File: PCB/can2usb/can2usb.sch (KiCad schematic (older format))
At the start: 36 parts, among them J1 STLINK, J2 Conn_01x03_Male, P1 USB_C_Plug_USB2.0, SW1 BOOT_SW, U1 STM32F103C6Tx, U2 TLP175A, U3 MCP2561-E-SN, U4 LM1117-3.3, U5 USBLC6-2SC6, Y1 16MHz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

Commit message: Finished brd
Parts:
- removed SW1: BOOT_SW, Button_Switch_SMD:SW_SPDT_PCM12, symbol Switch:SW_SPDT
- added H1, H2, H3: MountingHole, MountingHole:MountingHole_2.2mm_M2, symbol Mechanical:MountingHole
- added JP1: SolderJumper_3_Open, Jumper:SolderJumper-3_P1.3mm_Open_RoundedPad1.0x1.5mm, symbol Jumper:SolderJumper_3_Open
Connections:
- net +3V3: now also JP1.3 (B)
- net GND: now also JP1.1 (A)
- net at R8.2: now also JP1.2 (C)
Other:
- moved on the sheet: R8
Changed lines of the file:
@@
 L power:GND #PWR015
 U 1 1 63317619
-P 1100 6025
-F 0 "#PWR015" H 1100 5775 50  0001 C CNN
-F 1 "GND" V 1105 5897 50  0000 R CNN
-F 2 "" H 1100 6025 50  0001 C CNN
-F 3 "" H 1100 6025 50  0001 C CNN
-	1    1100 6025
+P 1125 6350
+F 0 "#PWR015" H 1125 6100 50  0001 C CNN
+F 1 "GND" V 1130 6222 50  0000 R CNN
+F 2 "" H 1125 6350 50  0001 C CNN
+F 3 "" H 1125 6350 50  0001 C CNN
+	1    1125 6350
 	0    1    1    0
 $EndComp
@@
 L power:+3.3V #PWR014
 U 1 1 63316E56
-P 1100 5825
-F 0 "#PWR014" H 1100 5675 50  0001 C CNN
-F 1 "+3.3V" V 1115 5953 50  0000 L CNN
-F 2 "" H 1100 5825 50  0001 C CNN
-F 3 "" H 1100 5825 50  0001 C CNN
-	1    1100 5825
-	0    -1   -1   0
-$EndComp
-Wire Wire Line
-	1500 5925 1550 5925
+P 1525 6350
+F 0 "#PWR014" H 1525 6200 50  0001 C CNN
+F 1 "+3.3V" V 1540 6478 50  0000 L CNN
+F 2 "" H 1525 6350 50  0001 C CNN
+F 3 "" H 1525 6350 50  0001 C CNN
+	1    1525 6350
+	0    1    1    0
+$EndComp
 $Comp
 L Device:R_Small R8
 U 1 1 6330E866
-P 1650 5925
-F 0 "R8" V 1454 5925 50  0000 C CNN
-F 1 "1k" V 1545 5925 50  0000 C CNN
-F 2 "Resistor_SMD:R_0805_2012Metric" H 1650 5925 50  0001 C CNN
-F 3 "~" H 1650 5925 50  0001 C CNN
-	1    1650 5925
-	0    1    1    0
-$EndComp
-$Comp
-L Switch:SW_SPDT SW1
-U 1 1 6330D3AE
-P 1300 5925
-F 0 "SW1" H 1300 5600 50  0000 C CNN
-F 1 "BOOT_SW" H 1300 5691 50  0000 C CNN
-F 2 "Button_Switch_SMD:SW_SPDT_PCM12" H 1300 5925 50  0001 C CNN
-F 3 "~" H 1300 5925 50  0001 C CNN
-	1    1300 5925
+P 1325 6600
+F 0 "R8" V 1129 6600 50  0000 C CNN
+F 1 "1k" V 1220 6600 50  0000 C CNN
+F 2 "Resistor_SMD:R_0805_2012Metric" H 1325 6600 50  0001 C CNN
+F 3 "~" H 1325 6600 50  0001 C CNN
+	1    1325 6600
 	-1   0    0    1
 $EndComp
@@
 Text GLabel 1475 1875 0    50   Input ~ 0
 BOOT0
-Text GLabel 1750 5925 2    50   Input ~ 0
+Text GLabel 1325 6700 3    50   Input ~ 0
 BOOT0
 Wire Notes Line
@@
 Text Notes 7100 6725 0    50   ~ 0
 USB2CAN - CAN TO UART TRANSLATION
+$Comp
+L Mechanical:MountingHole H1
+U 1 1 6349E742
+P 6625 5875
+F 0 "H1" H 6725 5921 50  0000 L CNN
+F 1 "MountingHole" H 6725 5830 50  0000 L CNN
+F 2 "MountingHole:MountingHole_2.2mm_M2" H 6625 5875 50  0001 C CNN
+F 3 "~" H 6625 5875 50  0001 C CNN
+	1    6625 5875
+	1    0    0    -1
+$EndComp
+$Comp
+L Mechanical:MountingHole H2
+U 1 1 6349F0A8
+P 6625 6225
+F 0 "H2" H 6725 6271 50  0000 L CNN
+F 1 "MountingHole" H 6725 6180 50  0000 L CNN
+F 2 "MountingHole:MountingHole_2.2mm_M2" H 6625 6225 50  0001 C CNN
+F 3 "~" H 6625 6225 50  0001 C CNN
+	1    6625 6225
+	1    0    0    -1
+$EndComp
+$Comp
+L Mechanical:MountingHole H3
+U 1 1 634CAEE0
+P 7650 5850
+F 0 "H3" H 7750 5896 50  0000 L CNN
+F 1 "MountingHole" H 7750 5805 50  0000 L CNN
+F 2 "MountingHole:MountingHole_2.2mm_M2" H 7650 5850 50  0001 C CNN
+F 3 "~" H 7650 5850 50  0001 C CNN
+	1    7650 5850
+	1    0    0    -1
+$EndComp
+$Comp
+L Jumper:SolderJumper_3_Open JP1
+U 1 1 635001D7
+P 1325 6350
+F 0 "JP1" H 1325 6555 50  0000 C CNN
+F 1 "SolderJumper_3_Open" H 1325 6464 50  0000 C CNN
+F 2 "Jumper:SolderJumper-3_P1.3mm_Open_RoundedPad1.0x1.5mm" H 1325 6350 50  0001 C CNN
+F 3 "~" H 1325 6350 50  0001 C CNN
+	1    1325 6350
+	1    0    0    -1
+$EndComp
 $EndSCHEMATC

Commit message: Minor chnages
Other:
- moved on the sheet: H3
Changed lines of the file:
@@
 L Mechanical:MountingHole H3
 U 1 1 634CAEE0
-P 7650 5850
-F 0 "H3" H 7750 5896 50  0000 L CNN
-F 1 "MountingHole" H 7750 5805 50  0000 L CNN
-F 2 "MountingHole:MountingHole_2.2mm_M2" H 7650 5850 50  0001 C CNN
-F 3 "~" H 7650 5850 50  0001 C CNN
-	1    7650 5850
+P 7500 5900
+F 0 "H3" H 7600 5946 50  0000 L CNN
+F 1 "MountingHole" H 7600 5855 50  0000 L CNN
+F 2 "MountingHole:MountingHole_2.2mm_M2" H 7500 5900 50  0001 C CNN
+F 3 "~" H 7500 5900 50  0001 C CNN
+	1    7500 5900
 	1    0    0    -1
 $EndComp

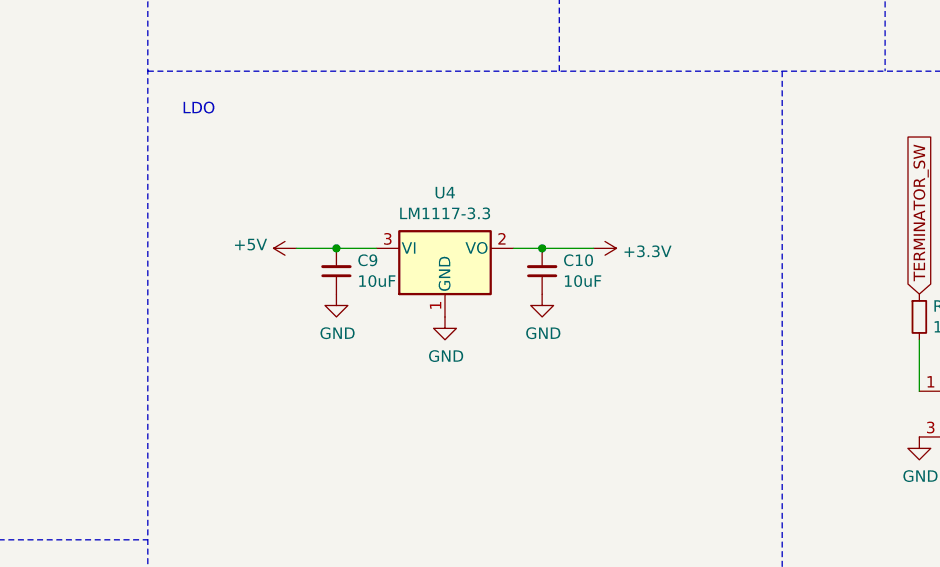
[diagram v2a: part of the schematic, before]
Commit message: New PCB design with 0402 and smaller LDO
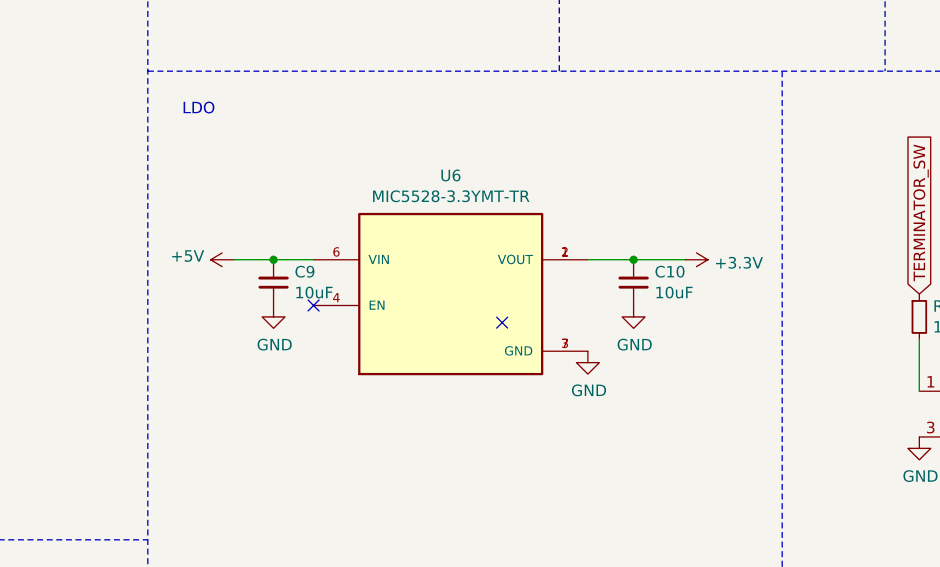
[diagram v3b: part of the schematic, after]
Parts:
- removed U4: LM1117-3.3, Package_TO_SOT_SMD:SOT-223-3_TabPin2, symbol Regulator_Linear:LM1117-3.3
- added U6: MIC5528-3.3YMT-TR, can2usb:SON40P120X120X60-7N, symbol can2usb_helper:MIC5528-3.3YMT-TR
- C1, C10, C2, C3, C4, C5, C6, C7, C8, C9: footprint Capacitor_SMD:C_0805_2012Metric -> Capacitor_SMD:C_0402_1005Metric_Pad0.74x0.62mm_HandSolder
- R1, R2, R3, R4, R5, R6, R7, R8, R_CONF1, R_CONF2, R_Terminator1: footprint Resistor_SMD:R_0805_2012Metric -> Resistor_SMD:R_0402_1005Metric_Pad0.72x0.64mm_HandSolder
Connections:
- net +3V3: now also U6.1 (VOUT), U6.2 (VOUT)
- net +5V: now also U6.6 (VIN)
- net GND: now also U6.3 (GND), U6.7 (GND)
- no-connect marks 27 -> 29
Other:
- moved on the sheet: C10, C9
